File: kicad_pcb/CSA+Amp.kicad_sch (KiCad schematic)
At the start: 25 parts, among them J301 CA probe, J302 RV Prob, U301 CR110, U302 TL071

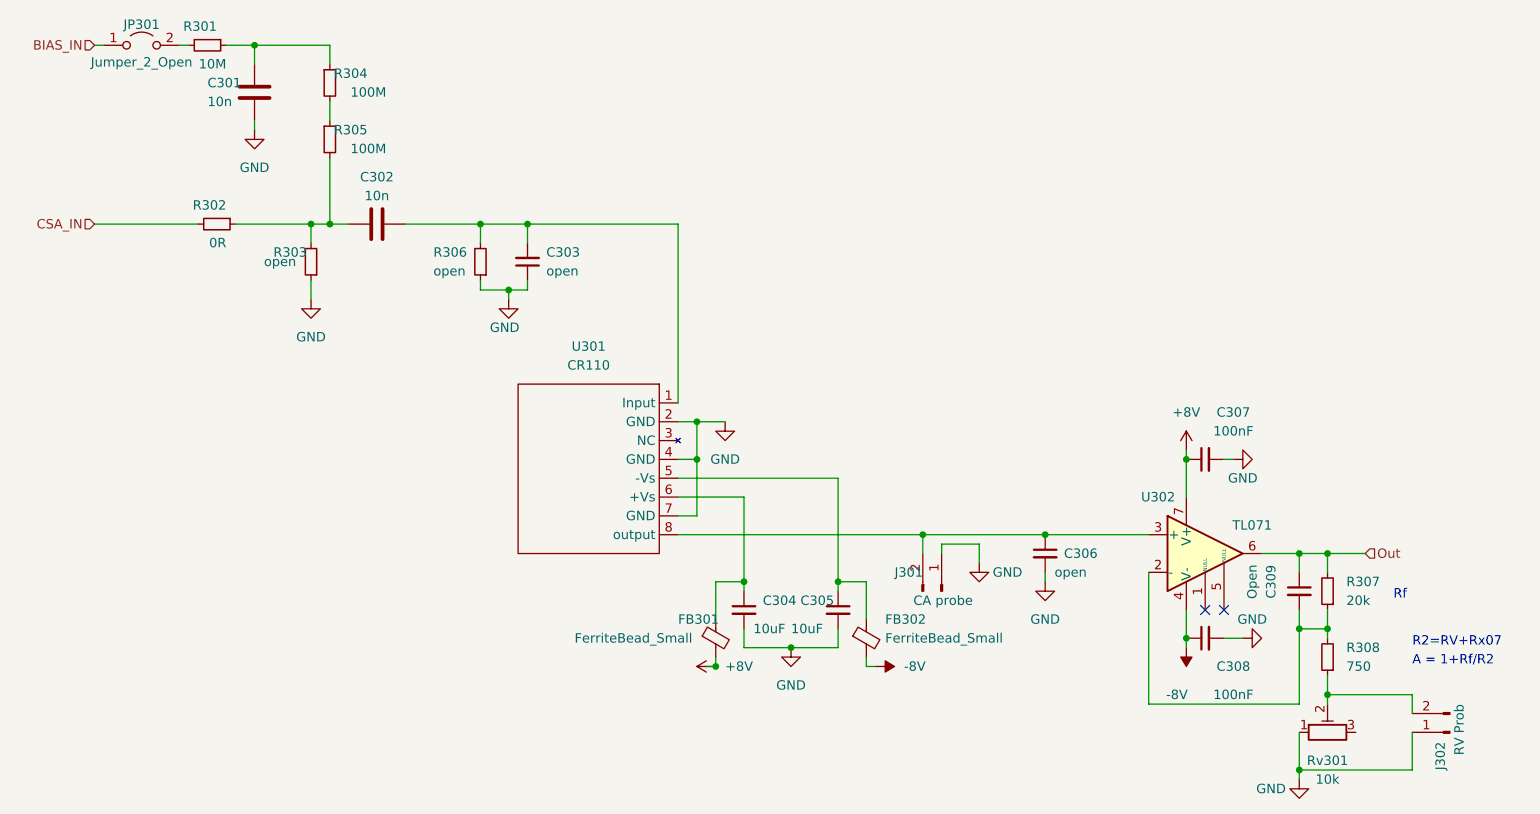
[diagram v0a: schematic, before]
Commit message: Update to KiCad 7. Added some freecad parts (unfortunately, thoroughly broken).
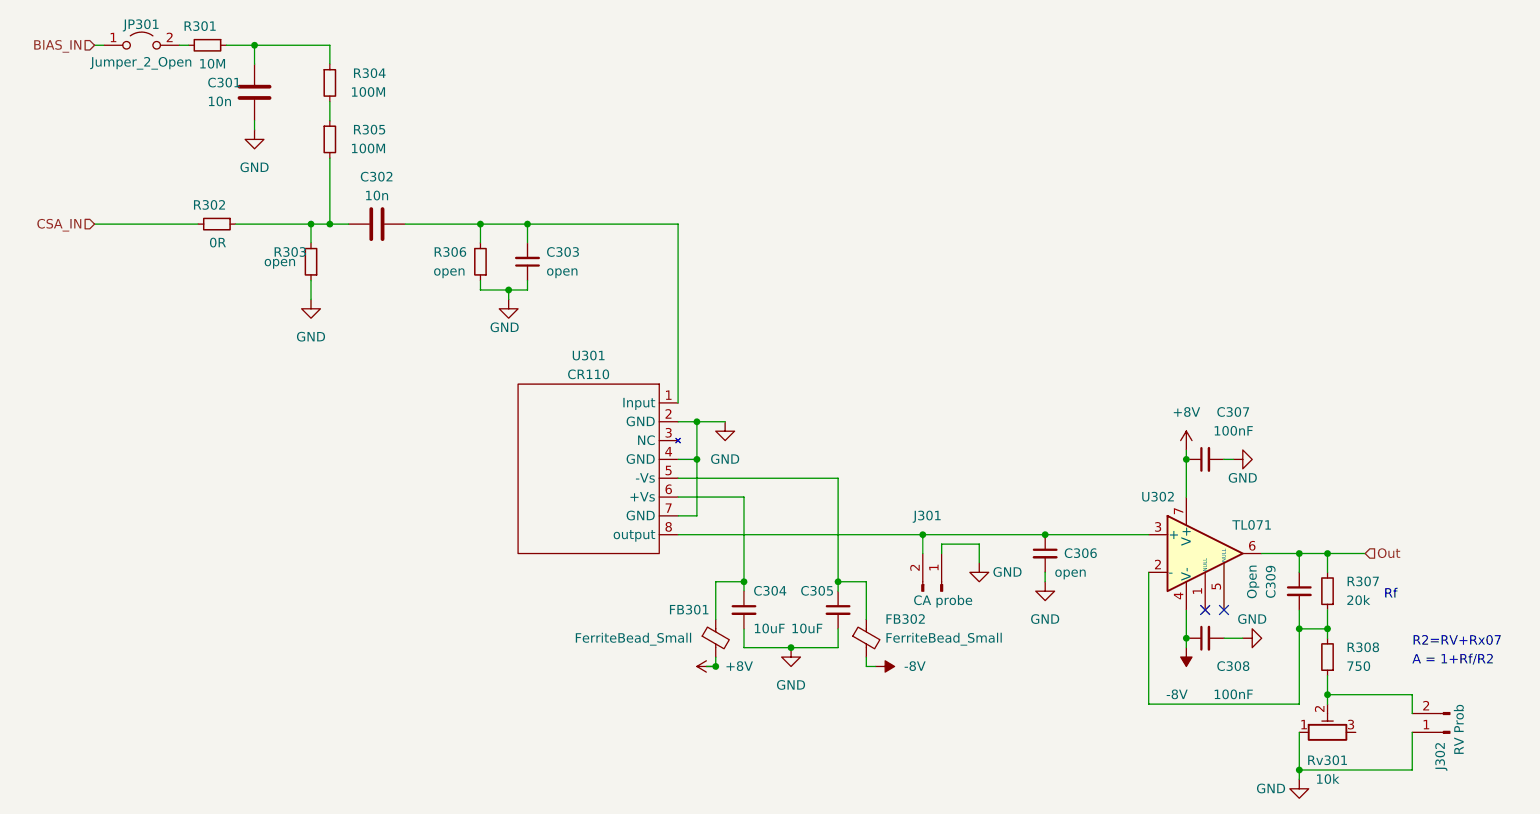
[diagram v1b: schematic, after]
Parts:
- J301, J302: symbol Connector:Conn_01x02_Male -> Connector:Conn_01x02_Pin
- U301: symbol ESC_Electronics:CR110 -> CrematModules:CR110
